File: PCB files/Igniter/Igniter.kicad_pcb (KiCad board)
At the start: 2 copper layers, 154.5 x 119.6 mm, 40 parts, among them IC1 74HC4050, J1 Micro_SD_Card, J2 Battery, J3 PT2, J4 PT1, J5 PT3, J6 PT4, J7 IgnitionCoil, Q1 N MOSFET, Q2 N MOSFET, Q3 N MOSFET, Q4 N MOSFET, Q5 N MOSFET, Q6 N MOSFET, U1 MIC5205-5.0

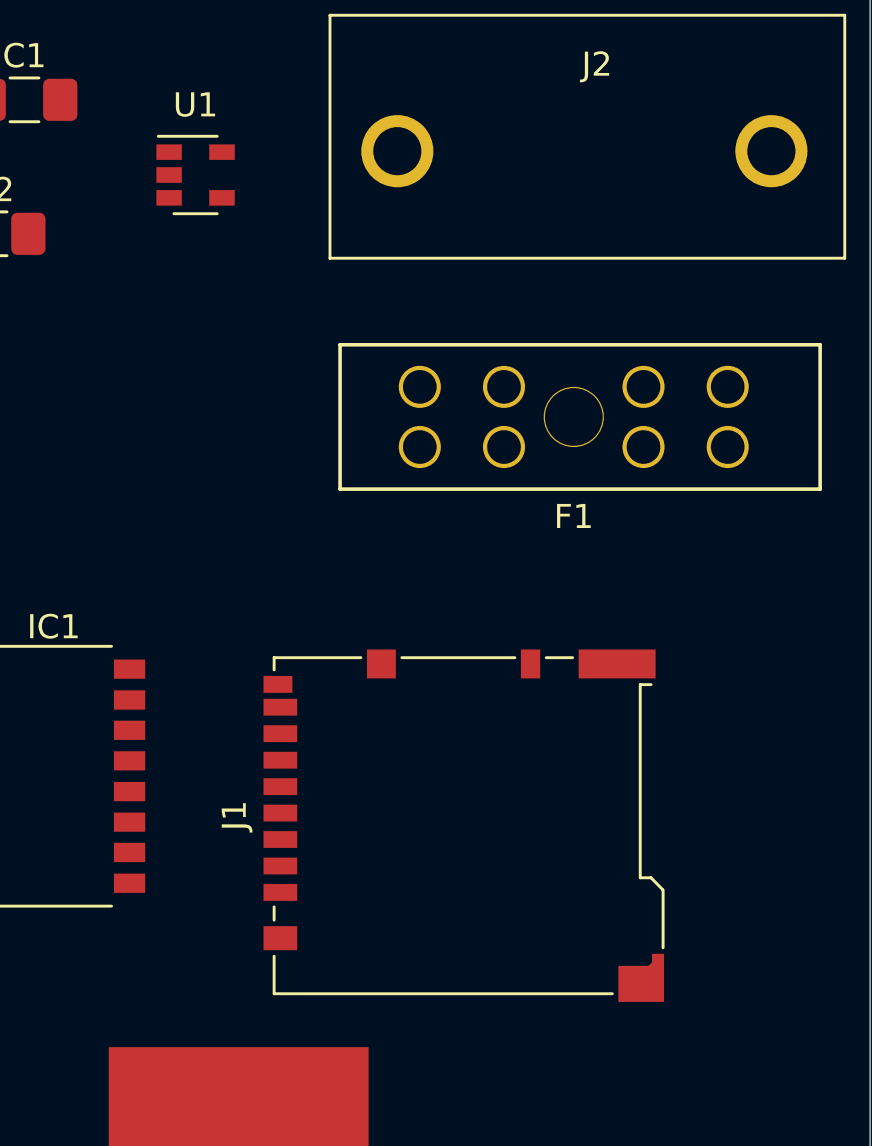
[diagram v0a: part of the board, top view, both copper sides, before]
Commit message: 11/9/2019
-Fixed regulator symbol
-Began adding solenoid valve indicators
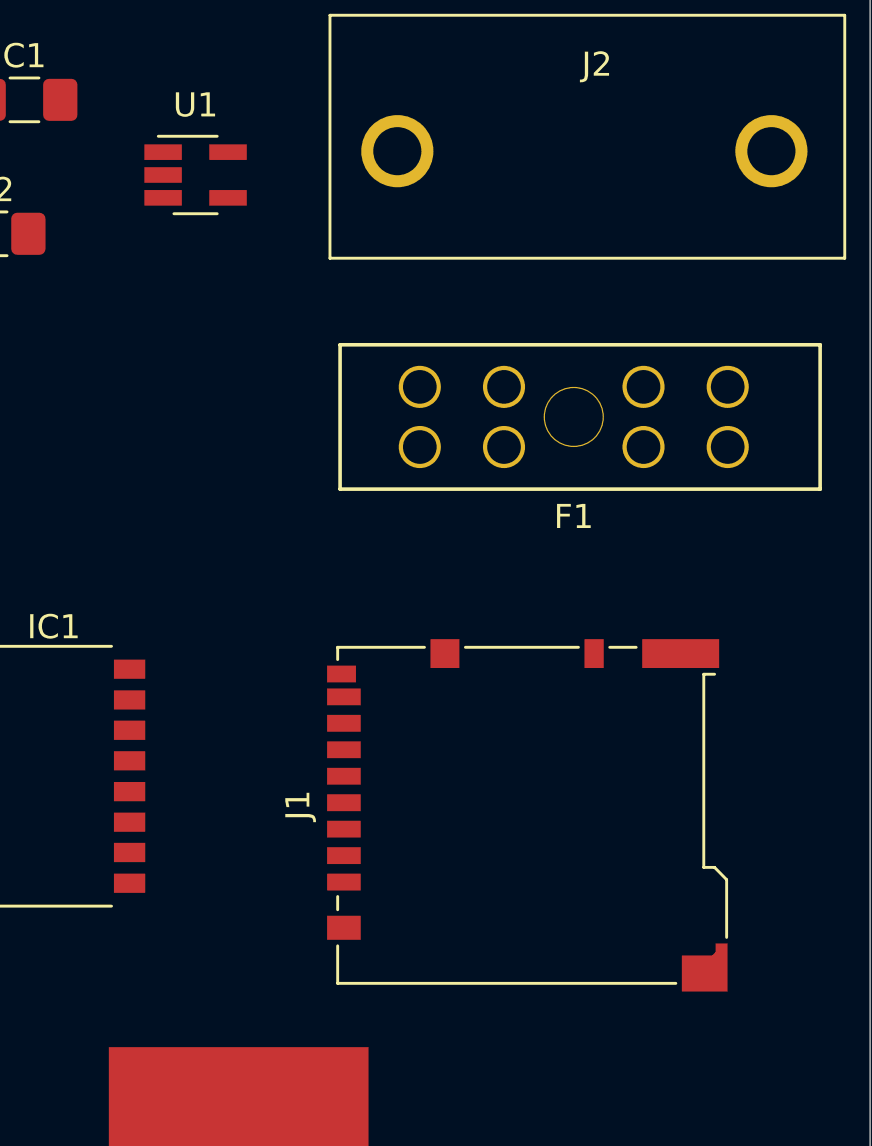
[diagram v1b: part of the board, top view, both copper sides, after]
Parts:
- U1: value MIC5205-5.0 -> MIC3490; footprint Package_TO_SOT_SMD:SOT-23-5 -> Package_TO_SOT_SMD:SOT-23-5_HandSoldering
- moved J1 2.68 mm to (225.3, 119.4)
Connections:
- C1 pad 1: +5V -> GNDREF
- C1 pad 2: GNDREF -> +5V
- F1 pad 2: Net-(F1-Pad2) -> (no net)
- IC1 pad 12: Net-(IC1-Pad12) -> (no net)
- IC1 pad 13: Net-(IC1-Pad13) -> (no net)
- IC1 pad 15: Net-(IC1-Pad15) -> (no net)
- IC1 pad 16: Net-(IC1-Pad16) -> (no net)
- J1 pad 1: Net-(J1-Pad1) -> (no net)
- J1 pad 8: Net-(J1-Pad8) -> (no net)
- J1 pad 9: Net-(J1-Pad9) -> (no net)
- J2 pad 1: Net-(J2-Pad1) -> (no net)
- U1 pad 4: +24V -> +5V
- U1 pad 5: +5V -> +24V
- XA1 pad 5V1: Net-(XA1-Pad5V1) -> (no net)
- XA1 pad 5V2: Net-(XA1-Pad5V2) -> (no net)
- XA1 pad 5V3: Net-(XA1-Pad5V3) -> (no net)
- XA1 pad 5V4: Net-(XA1-Pad5V4) -> (no net)
- XA1 pad A10: Net-(XA1-PadA10) -> (no net)
- XA1 pad A11: Net-(XA1-PadA11) -> (no net)
- XA1 pad A12: Net-(XA1-PadA12) -> (no net)
- XA1 pad A13: Net-(XA1-PadA13) -> (no net)
- XA1 pad A14: Net-(XA1-PadA14) -> (no net)
- XA1 pad A15: Net-(XA1-PadA15) -> (no net)
- XA1 pad A4: Net-(XA1-PadA4) -> (no net)
- XA1 pad A5: Net-(XA1-PadA5) -> (no net)
- XA1 pad A6: Net-(XA1-PadA6) -> (no net)
- XA1 pad A7: Net-(XA1-PadA7) -> (no net)
- XA1 pad A8: Net-(XA1-PadA8) -> (no net)
- XA1 pad A9: Net-(XA1-PadA9) -> (no net)
- XA1 pad AREF: Net-(XA1-PadAREF) -> (no net)
- XA1 pad D0: Net-(XA1-PadD0) -> (no net)
- XA1 pad D1: Net-(XA1-PadD1) -> (no net)
- XA1 pad D10: Net-(XA1-PadD10) -> (no net)
- XA1 pad D11: Net-(XA1-PadD11) -> (no net)
- XA1 pad D12: Net-(XA1-PadD12) -> (no net)
- XA1 pad D13: Net-(XA1-PadD13) -> (no net)
- XA1 pad D14: Net-(XA1-PadD14) -> (no net)
- XA1 pad D15: Net-(XA1-PadD15) -> (no net)
- XA1 pad D16: Net-(XA1-PadD16) -> (no net)
- XA1 pad D17: Net-(XA1-PadD17) -> (no net)
- XA1 pad D18: Net-(XA1-PadD18) -> (no net)
- XA1 pad D19: Net-(XA1-PadD19) -> (no net)
- XA1 pad D20: Net-(XA1-PadD20) -> (no net)
- XA1 pad D21: Net-(XA1-PadD21) -> (no net)
- XA1 pad D22: Net-(XA1-PadD22) -> (no net)
- XA1 pad D23: Net-(XA1-PadD23) -> (no net)
- XA1 pad D24: Net-(XA1-PadD24) -> (no net)
- XA1 pad D25: Net-(XA1-PadD25) -> (no net)
- XA1 pad D26: Net-(XA1-PadD26) -> (no net)
- XA1 pad D27: Net-(XA1-PadD27) -> (no net)
- XA1 pad D28: Net-(XA1-PadD28) -> (no net)
- XA1 pad D29: Net-(XA1-PadD29) -> (no net)
- XA1 pad D30: Net-(XA1-PadD30) -> (no net)
- XA1 pad D31: Net-(XA1-PadD31) -> (no net)
- XA1 pad D32: Net-(XA1-PadD32) -> (no net)
- XA1 pad D33: Net-(XA1-PadD33) -> (no net)
- XA1 pad D34: Net-(XA1-PadD34) -> (no net)
- XA1 pad D35: Net-(XA1-PadD35) -> (no net)
- XA1 pad D36: Net-(XA1-PadD36) -> (no net)
- XA1 pad D37: Net-(XA1-PadD37) -> (no net)
- XA1 pad D38: Net-(XA1-PadD38) -> (no net)
- XA1 pad D39: Net-(XA1-PadD39) -> (no net)
- XA1 pad D40: Net-(XA1-PadD40) -> (no net)
- XA1 pad D41: Net-(XA1-PadD41) -> (no net)
- XA1 pad D42: Net-(XA1-PadD42) -> (no net)
- XA1 pad D43: Net-(XA1-PadD43) -> (no net)
- XA1 pad D44: Net-(XA1-PadD44) -> (no net)
- XA1 pad D45: Net-(XA1-PadD45) -> (no net)
- XA1 pad D46: Net-(XA1-PadD46) -> (no net)
- XA1 pad D47: Net-(XA1-PadD47) -> (no net)
- XA1 pad D48: Net-(XA1-PadD48) -> (no net)
- XA1 pad D49: Net-(XA1-PadD49) -> (no net)
- XA1 pad D50: Net-(XA1-PadD50) -> (no net)
- XA1 pad D51: Net-(XA1-PadD51) -> (no net)
- XA1 pad D52: Net-(XA1-PadD52) -> (no net)
- XA1 pad D8: Net-(XA1-PadD8) -> (no net)
- XA1 pad D9: Net-(XA1-PadD9) -> (no net)
- XA1 pad IORF: Net-(XA1-PadIORF) -> (no net)
- XA1 pad RST1: Net-(XA1-PadRST1) -> (no net)
- XA1 pad RST2: Net-(XA1-PadRST2) -> (no net)
- XA1 pad SCL: Net-(XA1-PadSCL) -> (no net)
- XA1 pad SDA: Net-(XA1-PadSDA) -> (no net)
- XA1 pad VIN: Net-(XA1-PadVIN) -> (no net)

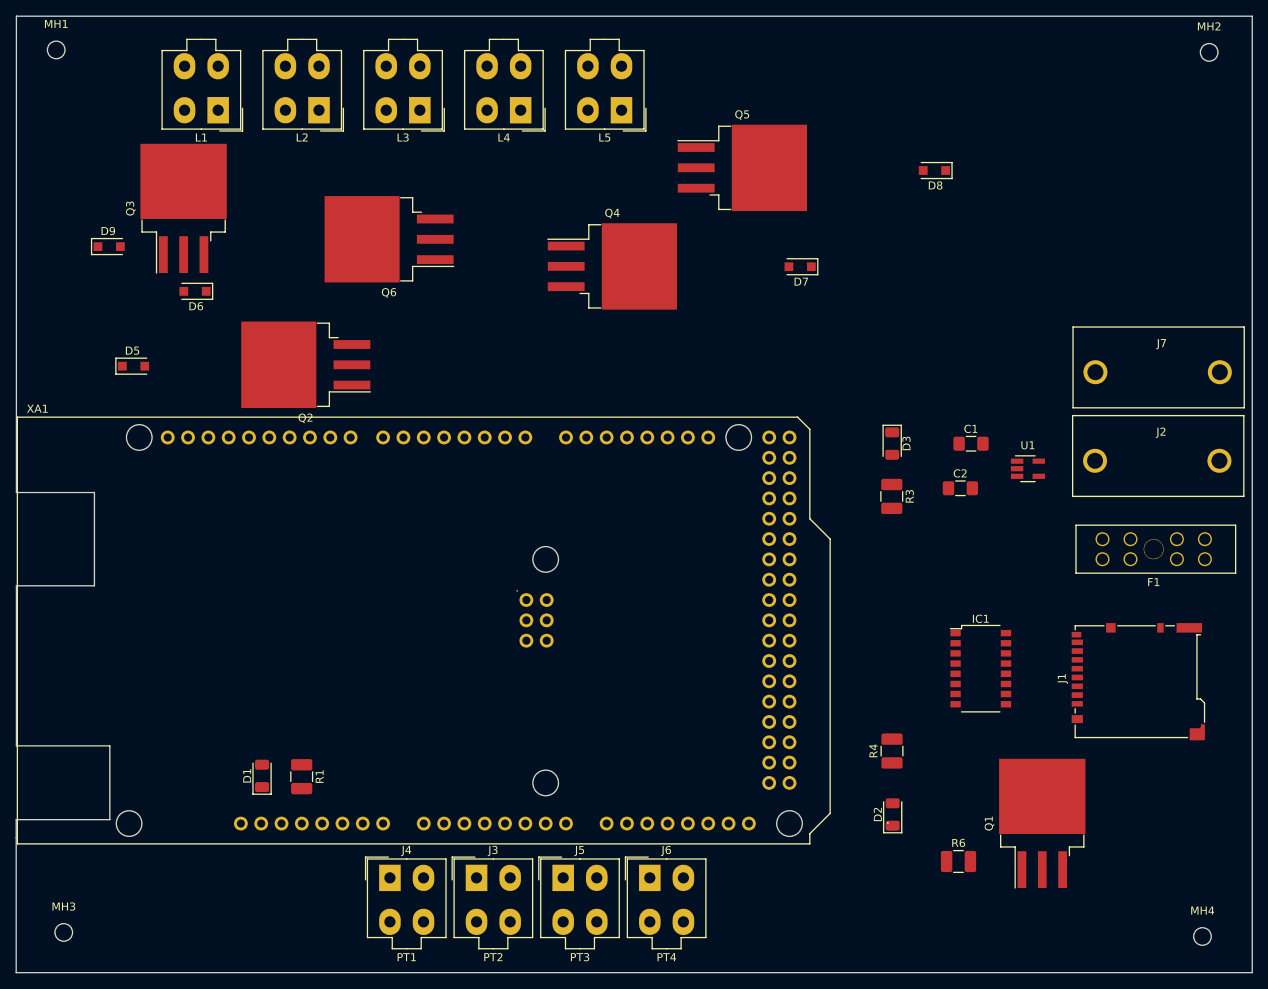
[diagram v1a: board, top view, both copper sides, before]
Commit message: 11/11/2019
-Organized footprints on the board layout
-Created blade fuse symbol
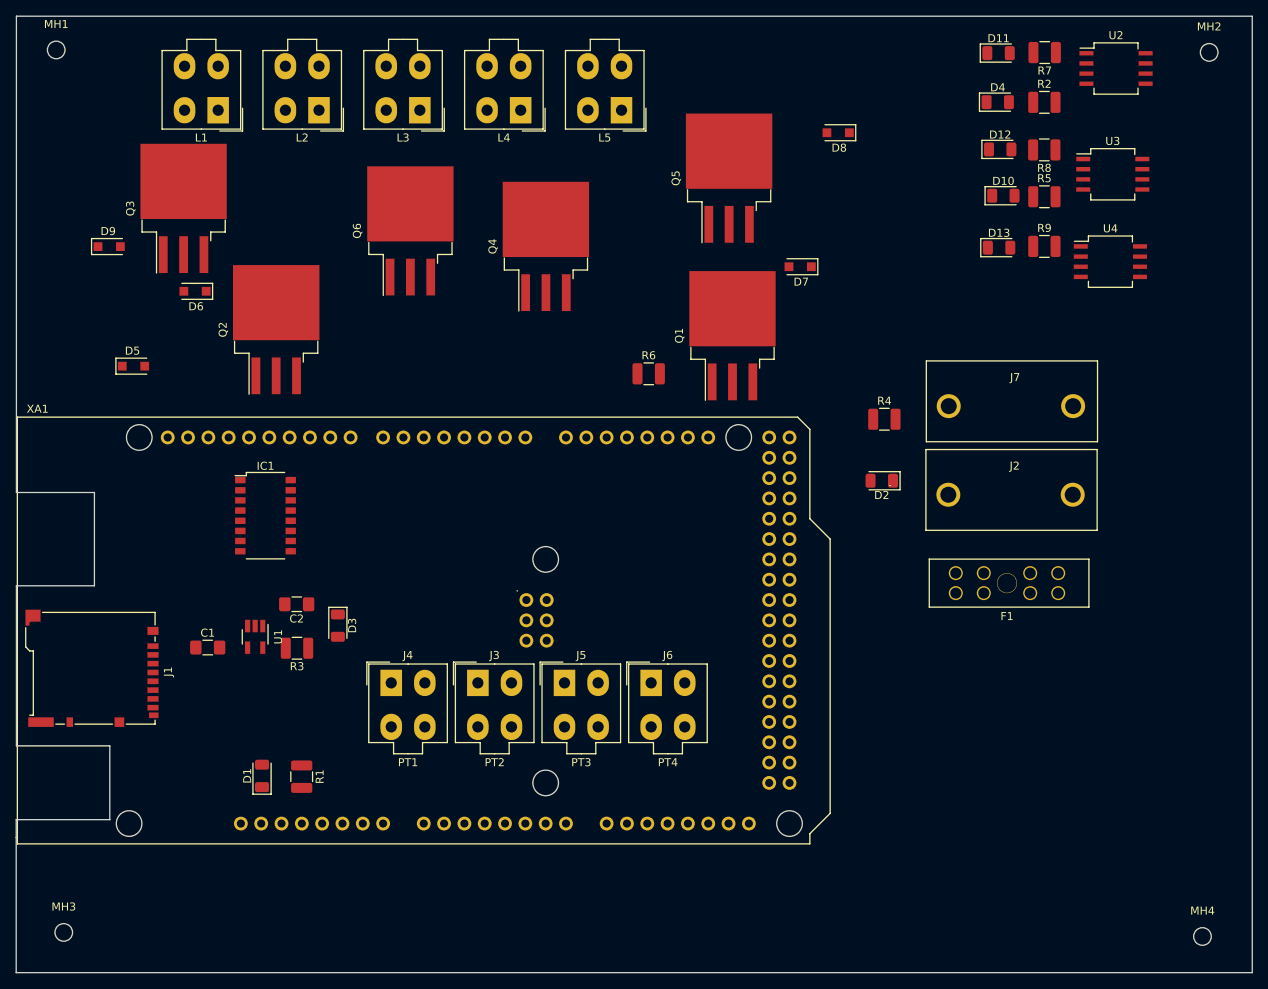
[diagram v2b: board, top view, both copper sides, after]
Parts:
- added D10: LED, LED_SMD:LED_1206_3216Metric, F.Cu at (208.5, 58.6)
- added D11: LED, LED_SMD:LED_1206_3216Metric, F.Cu at (207.9, 40.8)
- added D12: LED, LED_SMD:LED_1206_3216Metric, F.Cu at (208.1, 52.8)
- added D13: LED, LED_SMD:LED_1206_3216Metric, F.Cu at (207.9, 65.1)
- added D4: LED, LED_SMD:LED_1206_3216Metric, F.Cu at (207.8, 46.9)
- added R2: 1k2, Resistor_SMD:R_1210_3225Metric, F.Cu at (213.6, 46.9)
- added R5: 1k2, Resistor_SMD:R_1210_3225Metric, F.Cu at (213.6, 58.7)
- added R7: 1k2, Resistor_SMD:R_1210_3225Metric, F.Cu at (213.7, 40.7)
- added R8: 1k2, Resistor_SMD:R_1210_3225Metric, F.Cu at (213.6, 52.9)
- added R9: 1k2, Resistor_SMD:R_1210_3225Metric, F.Cu at (213.6, 64.9)
- added U2: FDS8984, Package_SO:SO-8_5.3x6.2mm_P1.27mm, F.Cu at (222.6, 42.7)
- added U3: FDS8984, Package_SO:SO-8_5.3x6.2mm_P1.27mm, F.Cu at (222.2, 55.9)
- added U4: FDS8984, Package_SO:SO-8_5.3x6.2mm_P1.27mm, F.Cu at (221.9, 66.9)
- R1, R3, R6: footprint Resistor_SMD:R_1210_3225Metric_Pad1.42x2.65mm_HandSolder -> Resistor_SMD:R_1210_3225Metric
- R4: value 1200 -> 1k2; footprint Resistor_SMD:R_1210_3225Metric_Pad1.42x2.65mm_HandSolder -> Resistor_SMD:R_1210_3225Metric
- moved J1 130.8 mm to (94.6, 117.7), turned to 270 degrees
- moved U1 98.9 mm to (115.0, 113.8), turned to 270 degrees
- moved C1 98.8 mm to (109.0, 115.1)
- moved IC1 91.4 mm to (116.3, 98.6)
- moved C2 84.2 mm to (120.2, 109.7), turned to 180 degrees
- moved R3 76.7 mm to (120.2, 115.2), turned to 180 degrees
- moved D3 72.9 mm to (125.3, 112.3)
- moved Q1 72.2 mm to (174.6, 76.1)
- moved R6 72.2 mm to (164.2, 80.9)
- moved D2 41.7 mm to (193.3, 94.2), turned to 180 degrees
- moved R4 41.5 mm to (193.6, 86.6), turned to 0 degrees
- moved J3 24.4 mm to (142.8, 119.5)
- moved J4 24.4 mm to (132.0, 119.5)
- moved J5 24.4 mm to (153.6, 119.5)
- moved J6 24.4 mm to (164.5, 119.5)
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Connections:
- net /solenoids/SOL1 renamed SOL1
- net /solenoids/SOL2 renamed SOL2
- net /solenoids/SOL3 renamed SOL3
- net /solenoids/SOL4 renamed SOL4
- net /solenoids/SOL5 renamed SOL5
- C1 pad 2: +5V -> +24V
- C2 pad 2: +24V -> +5V
- J3 pad 3: +5V -> +24V
- J4 pad 3: +5V -> +24V
- J5 pad 3: +5V -> +24V
- J6 pad 3: +5V -> +24V
- U1 pad 1: Net-(U1-Pad1) -> (no net)
- U1 pad 4: +5V -> +24V
- U1 pad 5: +24V -> +5V
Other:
- outline, holes or cut-outs redrawn

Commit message: 11/11/2019
-Completed addition of new blade fuse schematic symbol
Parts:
- F1: value Fuse -> BladeFuse
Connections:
- F1 pad 2: (no net) -> +24V
- F1 pad 3: (no net) -> +24V
- F1 pad 4: (no net) -> +24V
- F1 pad 5: (no net) -> Net-(F1-Pad5)
- F1 pad 6: (no net) -> Net-(F1-Pad5)
- F1 pad 7: (no net) -> Net-(F1-Pad5)
- F1 pad 8: (no net) -> Net-(F1-Pad5)
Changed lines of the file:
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@@
     (zones 0)
     (modules 53)
-    (nets 42)
+    (nets 43)
   )
   (page A4)
@@
   (net 40 "Net-(R8-Pad1)")
   (net 41 "Net-(R9-Pad1)")
+  (net 42 "Net-(F1-Pad5)")
   (net_class Default "This is the default net class."
     (clearance 0.2)
@@
     (add_net "Net-(D8-Pad2)")
     (add_net "Net-(D9-Pad2)")
+    (add_net "Net-(F1-Pad5)")
     (add_net "Net-(IC1-Pad10)")
     (add_net "Net-(IC1-Pad2)")
@@
       (effects (font (size 1 1) (thickness 0.15)))
     )
-    (fp_text value Fuse (at -0.0381 -3.8608) (layer F.Fab)
+    (fp_text value BladeFuse (at -0.0381 -3.8608) (layer F.Fab)
       (effects (font (size 1 1) (thickness 0.15)))
     )
@@
     (pad 1 thru_hole circle (at -6.4 -1.25 90) (size 1.75 1.75) (drill 1.4) (layers *.Cu *.Mask)
       (net 13 +24V))
-    (pad 2 thru_hole circle (at -2.9 -1.25 90) (size 1.75 1.75) (drill 1.4) (layers *.Cu *.Mask))
-    (pad 5 thru_hole circle (at 2.9 -1.25 90) (size 1.75 1.75) (drill 1.4) (layers *.Cu *.Mask))
-    (pad 6 thru_hole circle (at 6.4 -1.25 90) (size 1.75 1.75) (drill 1.4) (layers *.Cu *.Mask))
-    (pad 3 thru_hole circle (at -6.4 1.25 90) (size 1.75 1.75) (drill 1.4) (layers *.Cu *.Mask))
-    (pad 4 thru_hole circle (at -2.9 1.25 90) (size 1.75 1.75) (drill 1.4) (layers *.Cu *.Mask))
-    (pad 7 thru_hole circle (at 2.9 1.25 90) (size 1.75 1.75) (drill 1.4) (layers *.Cu *.Mask))
-    (pad 8 thru_hole circle (at 6.4 1.25 90) (size 1.75 1.75) (drill 1.4) (layers *.Cu *.Mask))
+    (pad 2 thru_hole circle (at -2.9 -1.25 90) (size 1.75 1.75) (drill 1.4) (layers *.Cu *.Mask)
+      (net 13 +24V))
+    (pad 5 thru_hole circle (at 2.9 -1.25 90) (size 1.75 1.75) (drill 1.4) (layers *.Cu *.Mask)
+      (net 42 "Net-(F1-Pad5)"))
+    (pad 6 thru_hole circle (at 6.4 -1.25 90) (size 1.75 1.75) (drill 1.4) (layers *.Cu *.Mask)
+      (net 42 "Net-(F1-Pad5)"))
+    (pad 3 thru_hole circle (at -6.4 1.25 90) (size 1.75 1.75) (drill 1.4) (layers *.Cu *.Mask)
+      (net 13 +24V))
+    (pad 4 thru_hole circle (at -2.9 1.25 90) (size 1.75 1.75) (drill 1.4) (layers *.Cu *.Mask)
+      (net 13 +24V))
+    (pad 7 thru_hole circle (at 2.9 1.25 90) (size 1.75 1.75) (drill 1.4) (layers *.Cu *.Mask)
+      (net 42 "Net-(F1-Pad5)"))
+    (pad 8 thru_hole circle (at 6.4 1.25 90) (size 1.75 1.75) (drill 1.4) (layers *.Cu *.Mask)
+      (net 42 "Net-(F1-Pad5)"))
   )
   (module Arduino:Arduino_Mega2560_Shield locked (layer F.Cu)
